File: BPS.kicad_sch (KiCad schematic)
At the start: 0 parts

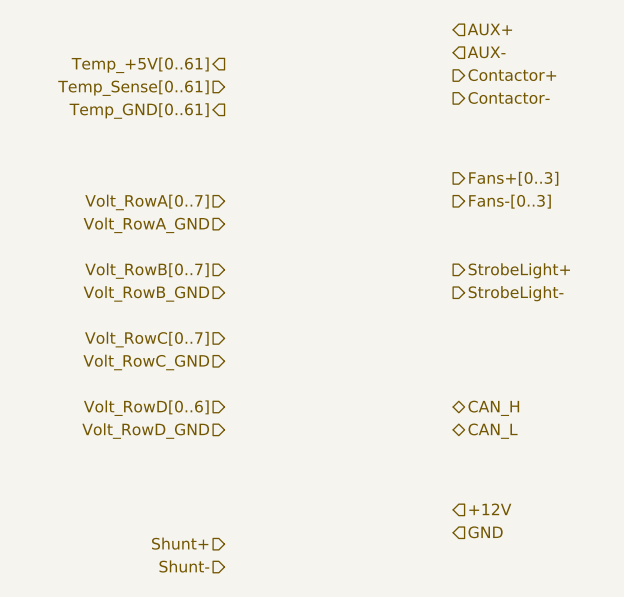
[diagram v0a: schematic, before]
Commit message: Updated Contactors, and fixed a few minor LV things
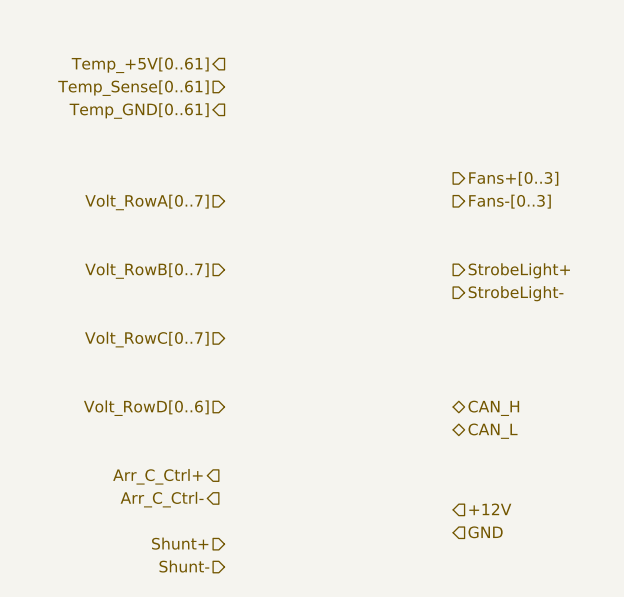
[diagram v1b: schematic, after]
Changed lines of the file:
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@@
-    (effects (font (size 1.27 1.27)) (justify right))
-  )
-  (hierarchical_label "Contactor-" (shape output) (at 114.3 58.42 0) (fields_autoplaced)
-    (effects (font (size 1.27 1.27)) (justify left))
-  )
-  (hierarchical_label "AUX+" (shape input) (at 114.3 50.8 0) (fields_autoplaced)
-    (effects (font (size 1.27 1.27)) (justify left))
-  )
-  (hierarchical_label "Volt_RowD_GND" (shape input) (at 88.9 95.25 180) (fields_autoplaced)
     (effects (font (size 1.27 1.27)) (justify right))
   )
@@
     (effects (font (size 1.27 1.27)) (justify left))
   )
-  (hierarchical_label "AUX-" (shape input) (at 114.3 53.34 0) (fields_autoplaced)
-    (effects (font (size 1.27 1.27)) (justify left))
-  )
   (hierarchical_label "Temp_GND[0..61]" (shape output) (at 88.9 59.69 180) (fields_autoplaced)
     (effects (font (size 1.27 1.27)) (justify right))
@@
     (effects (font (size 1.27 1.27)) (justify left))
   )
+  (hierarchical_label "Arr_C_Ctrl+" (shape output) (at 88.265 100.33 180) (fields_autoplaced)
+    (effects (font (size 1.27 1.27)) (justify right))
+  )
   (hierarchical_label "+12V" (shape input) (at 114.3 104.14 0) (fields_autoplaced)
     (effects (font (size 1.27 1.27)) (justify left))
-  )
-  (hierarchical_label "Volt_RowB_GND" (shape input) (at 88.9 80.01 180) (fields_autoplaced)
-    (effects (font (size 1.27 1.27)) (justify right))
   )
   (hierarchical_label "Volt_RowC[0..7]" (shape input) (at 88.9 85.09 180) (fields_autoplaced)
@@
     (effects (font (size 1.27 1.27)) (justify right))
   )
-  (hierarchical_label "Volt_RowA_GND" (shape input) (at 88.9 72.39 180) (fields_autoplaced)
-    (effects (font (size 1.27 1.27)) (justify right))
-  )
   (hierarchical_label "Volt_RowB[0..7]" (shape input) (at 88.9 77.47 180) (fields_autoplaced)
     (effects (font (size 1.27 1.27)) (justify right))
@@
     (effects (font (size 1.27 1.27)) (justify left))
   )
-  (hierarchical_label "Volt_RowC_GND" (shape input) (at 88.9 87.63 180) (fields_autoplaced)
+  (hierarchical_label "Arr_C_Ctrl-" (shape output) (at 88.265 102.87 180) (fields_autoplaced)
     (effects (font (size 1.27 1.27)) (justify right))
   )
-  (hierarchical_label "Contactor+" (shape output) (at 114.3 55.88 0) (fields_autoplaced)
-    (effects (font (size 1.27 1.27)) (justify left))
-  )
 )
